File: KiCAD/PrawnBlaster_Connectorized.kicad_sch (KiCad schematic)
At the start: 26 parts, among them IC1 74LVT245D,118, J2 Ext. Clock, J3 Ext. Trig., J4 Pseudoclock 3, J5 Pseudoclock 1, J6 Pseudoclock 2, J7 Pseudoclock 0, U2 74LVC1G34, U3 Pico, U4 74LVC1G17

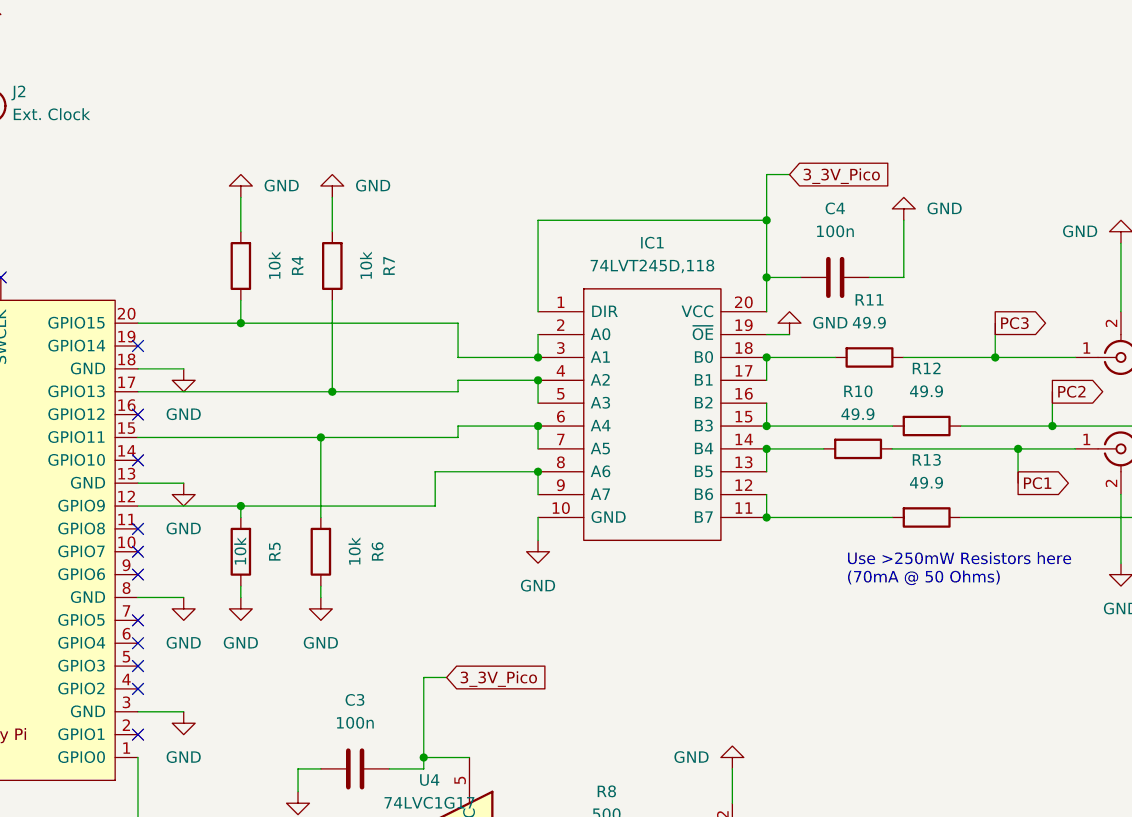
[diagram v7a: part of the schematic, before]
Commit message: Flipped buffer
.pcb:

   Flipped buffer so that pin one is in lower right and can connect to ground like on the prawnDO

  Modified resistor and track placements on all the connections on the buffer
       Routed pin 20 under the chip up
       to the 3V3 line as in PrawnDO

  Moved clk0 so that its trace could be a straight line

.sch:
  Changed the schematics to reflect the buffer being flipped and the new connections
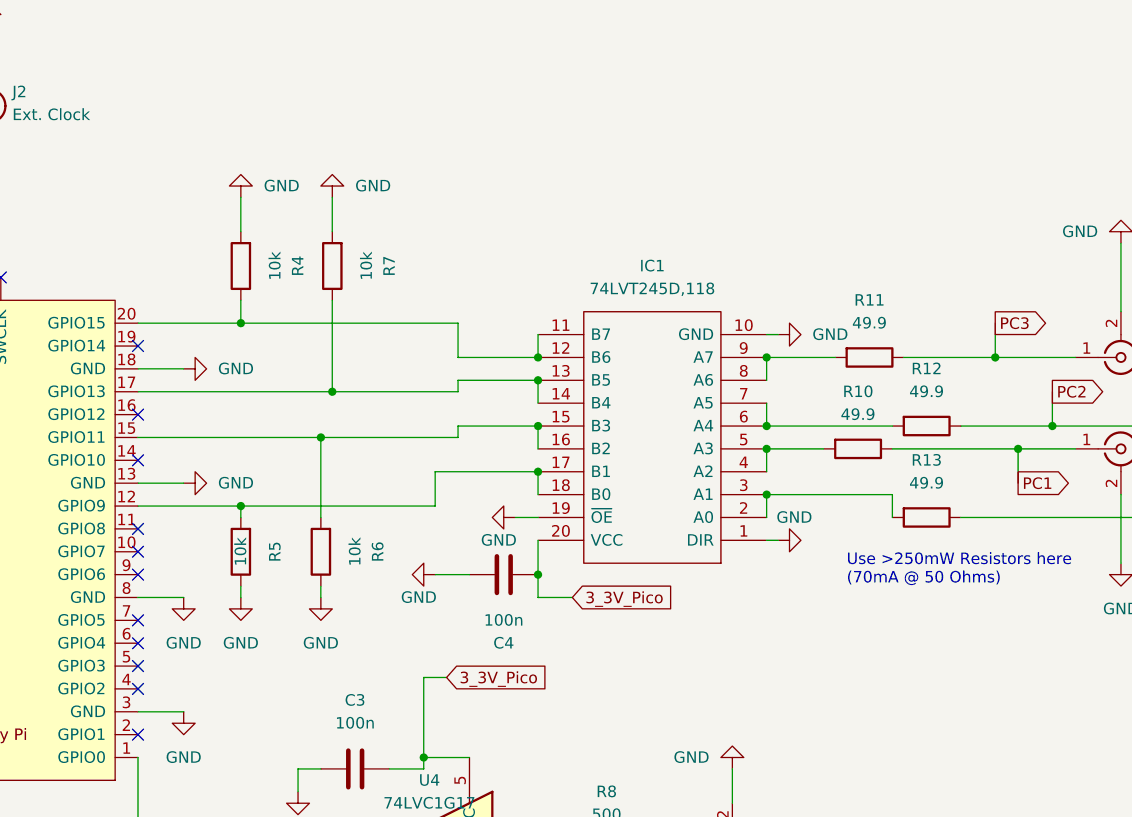
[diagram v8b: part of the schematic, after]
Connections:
- net 3_3V_Pico: no longer IC1.1 (DIR)
- net GND: now also IC1.1 (DIR)
- net at R6.2, U3.15 (GPIO11): now also IC1.15 (B3), IC1.16 (B2); no longer IC1.6 (A4), IC1.7 (A5)
- net at R5.2, U3.12 (GPIO9): now also IC1.17 (B1), IC1.18 (B0); no longer IC1.8 (A6), IC1.9 (A7)
- net at R7.1, U3.17 (GPIO13): now also IC1.13 (B5), IC1.14 (B4); no longer IC1.4 (A2), IC1.5 (A3)
- net at R4.1, U3.20 (GPIO15): now also IC1.11 (B7), IC1.12 (B6); no longer IC1.2 (A0), IC1.3 (A1)
- new net: IC1.8 (A6), IC1.9 (A7), R11.2
- new net: IC1.6 (A4), IC1.7 (A5), R12.2
- new net: IC1.4 (A2), IC1.5 (A3), R10.2
- new net: IC1.2 (A0), IC1.3 (A1), R13.2
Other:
- moved on the sheet: C4, IC1
